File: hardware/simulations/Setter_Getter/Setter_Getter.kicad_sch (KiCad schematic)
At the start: 23 parts, among them Q101 2N7000, U101 LM393

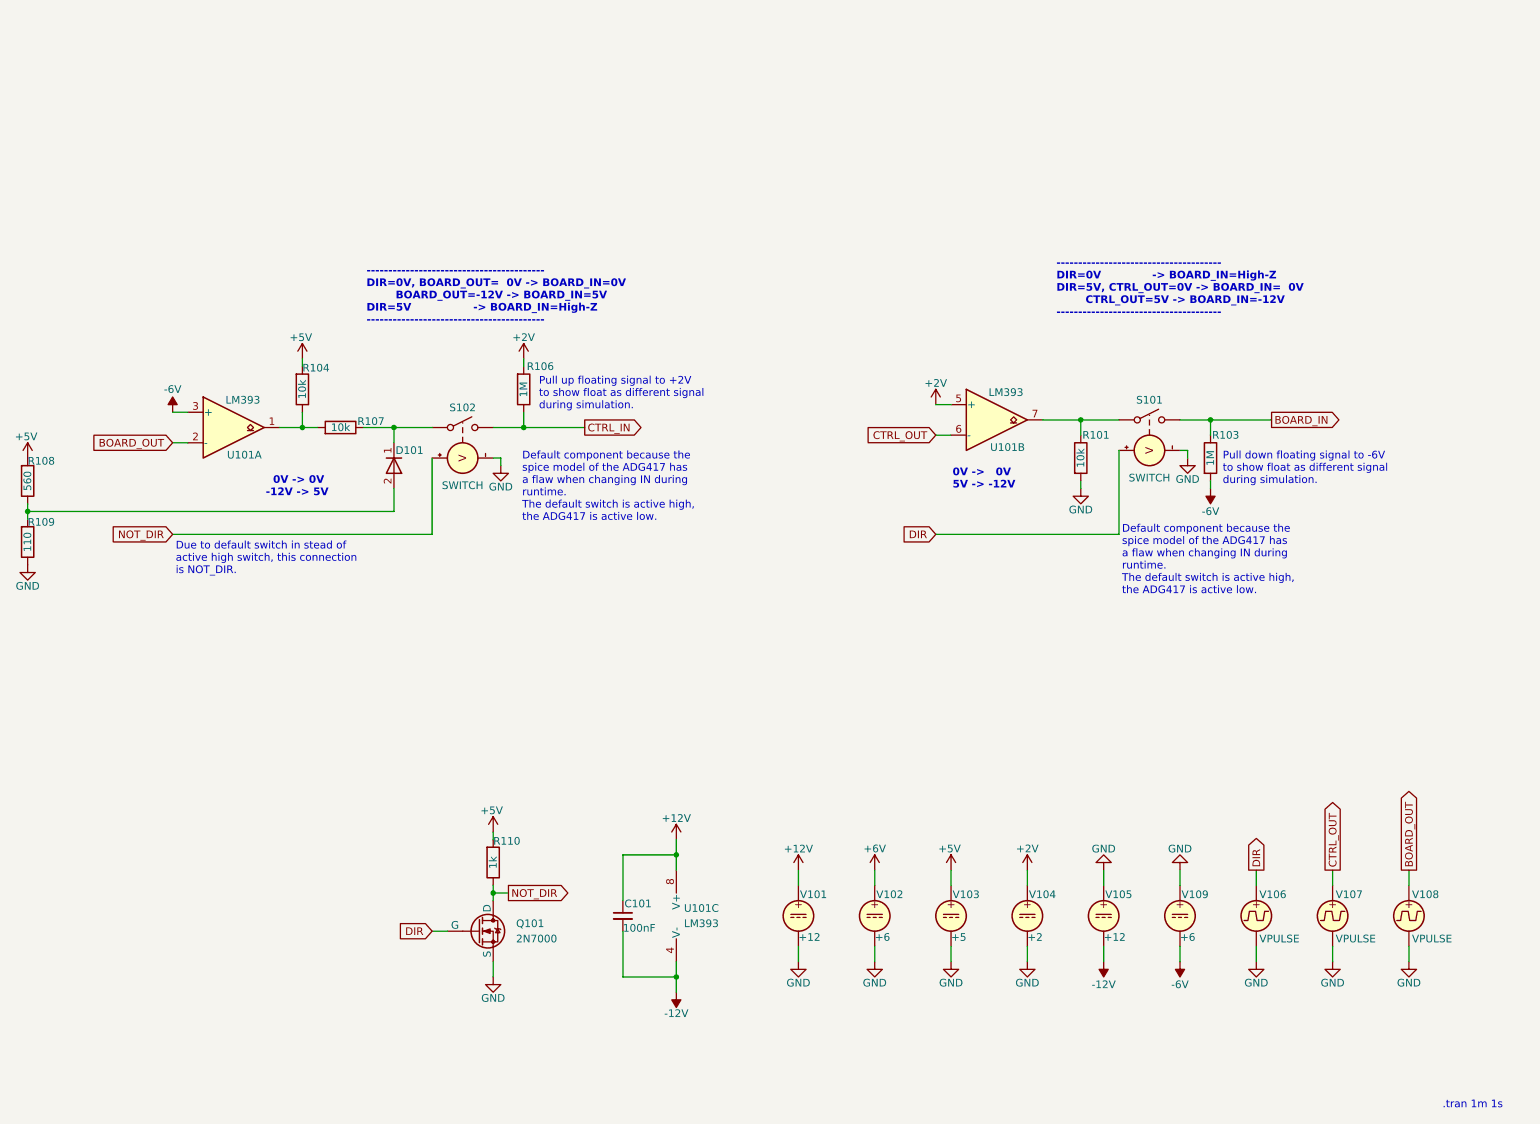
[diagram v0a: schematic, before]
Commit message: Verification board under test input impedance done (at most 3.64mA)
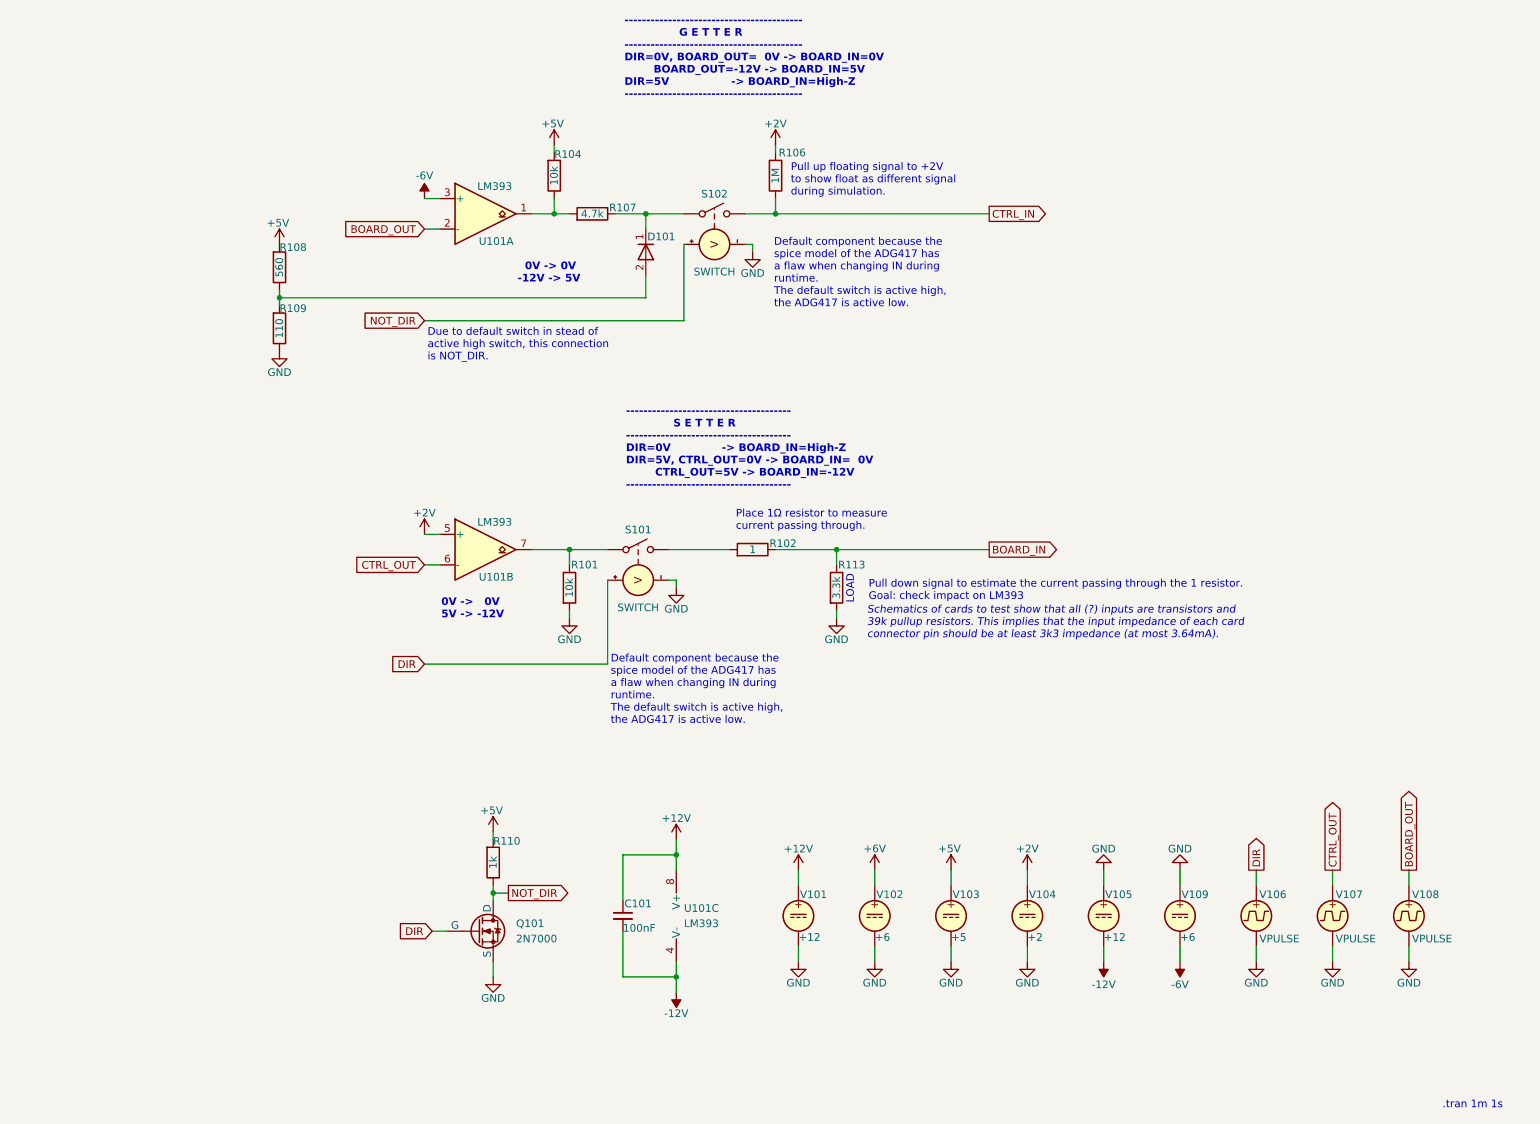
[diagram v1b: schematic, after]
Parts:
- removed R103: 1M, Resistor_THT:R_Axial_DIN0207_L6.3mm_D2.5mm_P7.62mm_Horizontal, symbol Device:R
- added R102: 1, Resistor_THT:R_Axial_DIN0207_L6.3mm_D2.5mm_P7.62mm_Horizontal, symbol Device:R
- added R113: 3.3k, Resistor_THT:R_Axial_DIN0207_L6.3mm_D2.5mm_P7.62mm_Horizontal, symbol Device:R
- R107: value 10k -> 4.7k
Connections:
- net BOARD_IN: now also R102.1, R113.1; no longer S101.2 (N-)
- net GND: now also R113.2
- new net: R102.2, S101.2 (N-)
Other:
- note added: "-------------------------------------- S E T T E R -------------------------------------- DIR=0V -> BOARD_IN=High-Z DIR=5V, CTRL_OUT=0V -> BOARD_IN= 0V CTRL_OUT=5V -> BOARD_IN=-12V --------------------------------------"
- note added: "----------------------------------------- G E T T E R ----------------------------------------- DIR=0V, BOARD_OUT= 0V -> BOARD_IN=0V BOARD_OUT=-12V -> BOARD_IN=5V DIR=5V -> BOARD_IN=High-Z -----------------------------------------"
- note added: "LOAD"
- note added: "Place 1Ω resistor to measure current passing through."
- note added: "Pull down signal to estimate the current passing through the 1 resistor. Goal: check impact on LM393"
- note added: "Schematics of cards to test show that all (?) inputs are transistors and 39k pullup resistors. This implies that the input impedance of each card connector pin should be at least 3k3 impedance (at most 3.64mA)."
- note removed: "-------------------------------------- DIR=0V -> BOARD_IN=High-Z DIR=5V, CTRL_OUT=0V -> BOARD_IN= 0V CTRL_OUT=5V -> BOARD_IN=-12V --------------------------------------"
- note removed: "----------------------------------------- DIR=0V, BOARD_OUT= 0V -> BOARD_IN=0V BOARD_OUT=-12V -> BOARD_IN=5V DIR=5V -> BOARD_IN=High-Z -----------------------------------------"
- note removed: "Pull down floating signal to -6V to show float as different signal during simulation."
- moved on the sheet: D101, R101, R104, R106, R107, R108, R109, S101, S102, U101A, U101B

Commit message: Added Setter_Getter proof of concept and Setter_Getter 74xx165 and 74xx595 integration proof of concept
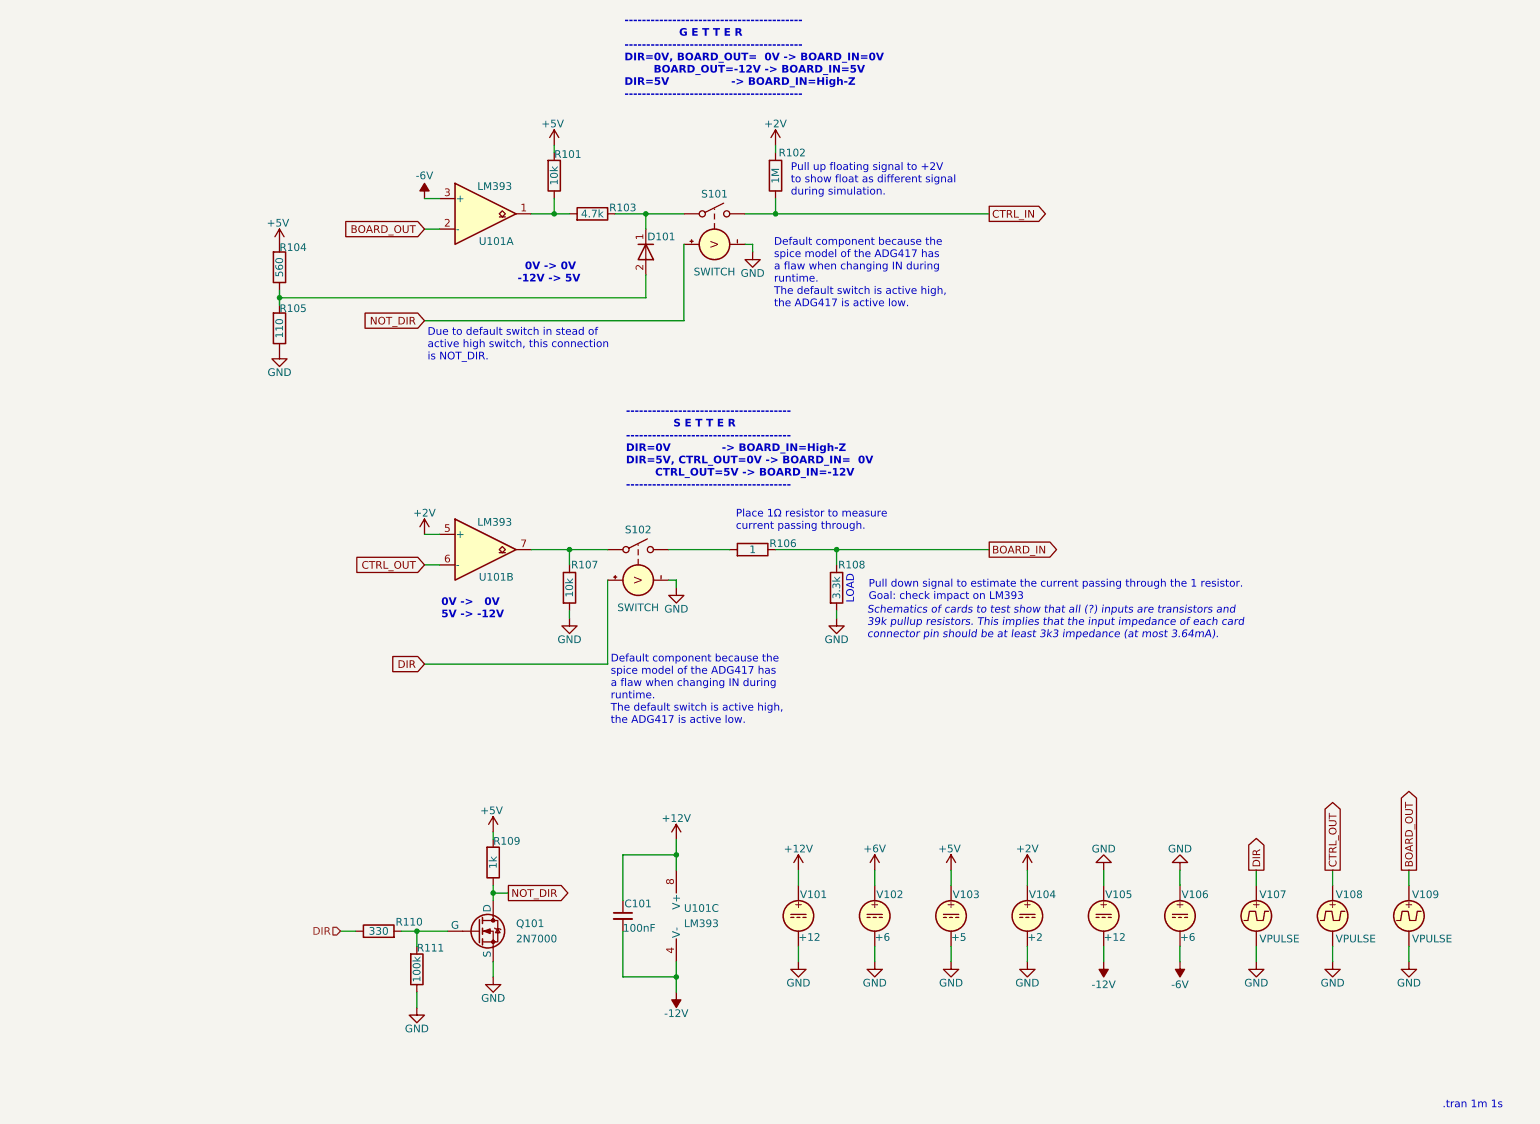
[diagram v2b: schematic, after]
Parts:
- added R110: 330, Resistor_THT:R_Axial_DIN0207_L6.3mm_D2.5mm_P7.62mm_Horizontal, symbol Device:R
- added R111: 100k, Resistor_THT:R_Axial_DIN0207_L6.3mm_D2.5mm_P7.62mm_Horizontal, symbol Device:R
- renumbered R104 to R101, R106 to R102, R107 to R103, R108 to R104, R109 to R105, R102 to R106, R101 to R107, R113 to R108, R110 to R109, S102 to S101, S101 to S102, V109 to V106, V106 to V107, V107 to V108, V108 to V109
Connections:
- net DIR: now also R110.1; no longer Q101.2 (G)
- net GND: now also R111.1
- new net: Q101.2 (G), R110.2, R111.2

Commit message: File cleanup
Added final schematics
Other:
- note added: "Default component because sometimes a switch is just a switch."
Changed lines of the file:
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@@
 		)
 	)
-	(text "Default component because the\nspice model of the ADG417 has\na flaw when changing IN during\nruntime.\nThe default switch is active high,\nthe ADG417 is active low."
+	(text "Default component because\nsometimes a switch is just\na switch."
 		(exclude_from_sim no)
 		(at 161.036 52.324 0)
